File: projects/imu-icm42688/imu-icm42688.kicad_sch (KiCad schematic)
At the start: 14 parts, among them J1 HEADER, U1 AP2112K-3.3, U2 ICM-42688-P

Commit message: PCB workspace: scoped escape hatch, hardened gates, repo cleanup
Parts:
- removed C4: 100nF, Capacitor_SMD:C_0402_1005Metric, symbol Device:C
- removed C5: 1uF, Capacitor_SMD:C_0402_1005Metric, symbol Device:C
- removed J1: HEADER, Connector_PinHeader_2.54mm:PinHeader_1x10_P2.54mm_Vertical, symbol Connector_Generic:Conn_01x10
- removed R1, R2: 4.7k, Resistor_SMD:R_0402_1005Metric, symbol Device:R
- removed U1: AP2112K-3.3, Package_TO_SOT_SMD:SOT-23-5, symbol Regulator_Linear:AP2112K-3.3
- removed U2: ICM-42688-P, symbol Connector_Generic:Conn_01x14
- added J1: SPI-HDR, Connector_PinHeader_2.54mm:PinHeader_1x06_P2.54mm_Vertical, symbol Connector_Generic:Conn_01x06
- added TP3: INT1, TestPoint:TestPoint_Pad_1.0x1.0mm, symbol Connector_Generic:Conn_01x01
- added U1: ICM-42688-P, jlcpcb:LGA-14_L3.0-W2.5-P0.50-TL, symbol jlcpcb:ICM-42688-P
- C1: value 1uF -> 100nF
- C2: value 1uF -> 2.2uF; footprint Capacitor_SMD:C_0402_1005Metric -> Capacitor_SMD:C_0603_1608Metric
- C3: value 100nF -> 10nF
- H1, H2: value MH -> M2
- TP1: value TP_3V3 -> +3V3
- TP2: value TP_GND -> GND
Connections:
- net +3V3: now also C1.1, C2.1, C3.1, TP1.1 (Pin_1), J1.1 (Pin_1), U1.5 (VDDIO), U1.8 (VDD)
- net GND: now also C1.2, C2.2, C3.2, TP2.1 (Pin_1), J1.2 (Pin_2), U1.6 (GND), U1.7 (RESV), U1.9 (INT2/FSYNC/CLKIN)
- net INT1: now also TP3.1 (Pin_1), U1.4 (INT1/INT)
- new net SPI_CS: J1.6 (Pin_6), U1.12 (AP_CS)
- new net SPI_SCLK: J1.3 (Pin_3), U1.13 (AP_SCL/AP_SCLK)
- new net SPI_SDI: J1.4 (Pin_4), U1.14 (AP_SDA/AP_SDIO/AP_SDI)
- new net SPI_SDO: J1.5 (Pin_5), U1.1 (AP_SDO/AP_AD0)
- no-connect marks 0 -> 6

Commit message: 9/6 update
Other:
- company: (none) -> PSI Rocketry
- title: (none) -> IMU Breakout - ICM-42688-P
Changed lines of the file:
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@@
 	(generator_version "0.1")
 	(paper "A4")
+	(title_block
+		(title "IMU Breakout - ICM-42688-P")
+		(date "2026-08-24")
+		(rev "1")
+		(company "PSI Rocketry")
+		(comment 1 "Lee Taeho")
+	)
 	(sheet_instances
 		(path "/"
@@
 		(instances
 			(project "imu-icm42688"
-				(path "/b2c1d009-25c1-4b62-a2bc-4ddaf3d245d5"
+				(path "/22f1c0e7-3e2a-45f0-97f5-2cd534b13261"
 					(reference "U1")
 					(unit 1)
@@
 		(instances
 			(project "imu-icm42688"
-				(path "/b2c1d009-25c1-4b62-a2bc-4ddaf3d245d5"
+				(path "/22f1c0e7-3e2a-45f0-97f5-2cd534b13261"
 					(reference "#PWR101")
 					(unit 1)
@@
 		(instances
 			(project "imu-icm42688"
-				(path "/b2c1d009-25c1-4b62-a2bc-4ddaf3d245d5"
+				(path "/22f1c0e7-3e2a-45f0-97f5-2cd534b13261"
 					(reference "#PWR102")
 					(unit 1)
@@
 		(instances
 			(project "imu-icm42688"
-				(path "/b2c1d009-25c1-4b62-a2bc-4ddaf3d245d5"
+				(path "/22f1c0e7-3e2a-45f0-97f5-2cd534b13261"
 					(reference "#PWR103")
 					(unit 1)
@@
 		(instances
 			(project "imu-icm42688"
-				(path "/b2c1d009-25c1-4b62-a2bc-4ddaf3d245d5"
+				(path "/22f1c0e7-3e2a-45f0-97f5-2cd534b13261"
 					(reference "#PWR104")
 					(unit 1)
@@
 		(instances
 			(project "imu-icm42688"
-				(path "/b2c1d009-25c1-4b62-a2bc-4ddaf3d245d5"
+				(path "/22f1c0e7-3e2a-45f0-97f5-2cd534b13261"
 					(reference "#PWR105")
 					(unit 1)
@@
 		(instances
 			(project "imu-icm42688"
-				(path "/b2c1d009-25c1-4b62-a2bc-4ddaf3d245d5"
+				(path "/22f1c0e7-3e2a-45f0-97f5-2cd534b13261"
 					(reference "C1")
 					(unit 1)
@@
 		(instances
 			(project "imu-icm42688"
-				(path "/b2c1d009-25c1-4b62-a2bc-4ddaf3d245d5"
+				(path "/22f1c0e7-3e2a-45f0-97f5-2cd534b13261"
 					(reference "#PWR106")
 					(unit 1)
@@
 		(instances
 			(project "imu-icm42688"
-				(path "/b2c1d009-25c1-4b62-a2bc-4ddaf3d245d5"
+				(path "/22f1c0e7-3e2a-45f0-97f5-2cd534b13261"
 					(reference "#PWR107")
 					(unit 1)
@@
 		(instances
 			(project "imu-icm42688"
-				(path "/b2c1d009-25c1-4b62-a2bc-4ddaf3d245d5"
+				(path "/22f1c0e7-3e2a-45f0-97f5-2cd534b13261"
 					(reference "C2")
 					(unit 1)
@@
 		(instances
 			(project "imu-icm42688"
-				(path "/b2c1d009-25c1-4b62-a2bc-4ddaf3d245d5"
+				(path "/22f1c0e7-3e2a-45f0-97f5-2cd534b13261"
 					(reference "#PWR108")
 					(unit 1)
@@
 		(instances
 			(project "imu-icm42688"
-				(path "/b2c1d009-25c1-4b62-a2bc-4ddaf3d245d5"
+				(path "/22f1c0e7-3e2a-45f0-97f5-2cd534b13261"
 					(reference "#PWR109")
 					(unit 1)
@@
 		(instances
 			(project "imu-icm42688"
-				(path "/b2c1d009-25c1-4b62-a2bc-4ddaf3d245d5"
+				(path "/22f1c0e7-3e2a-45f0-97f5-2cd534b13261"
 					(reference "C3")
 					(unit 1)
@@
 		(instances
 			(project "imu-icm42688"
-				(path "/b2c1d009-25c1-4b62-a2bc-4ddaf3d245d5"
+				(path "/22f1c0e7-3e2a-45f0-97f5-2cd534b13261"
 					(reference "#PWR110")
 					(unit 1)
@@
 		(instances
 			(project "imu-icm42688"
-				(path "/b2c1d009-25c1-4b62-a2bc-4ddaf3d245d5"
+				(path "/22f1c0e7-3e2a-45f0-97f5-2cd534b13261"
 					(reference "#PWR111")
 					(unit 1)
@@
 		(instances
 			(project "imu-icm42688"
-				(path "/b2c1d009-25c1-4b62-a2bc-4ddaf3d245d5"
+				(path "/22f1c0e7-3e2a-45f0-97f5-2cd534b13261"
 					(reference "J1")
 					(unit 1)
@@
 		(instances
 			(project "imu-icm42688"
-				(path "/b2c1d009-25c1-4b62-a2bc-4ddaf3d245d5"
+				(path "/22f1c0e7-3e2a-45f0-97f5-2cd534b13261"
 					(reference "#PWR112")
 					(unit 1)
@@
 		(instances
 			(project "imu-icm42688"
-				(path "/b2c1d009-25c1-4b62-a2bc-4ddaf3d245d5"
+				(path "/22f1c0e7-3e2a-45f0-97f5-2cd534b13261"
 					(reference "#PWR113")
 					(unit 1)
@@
 		(instances
 			(project "imu-icm42688"
-				(path "/b2c1d009-25c1-4b62-a2bc-4ddaf3d245d5"
+				(path "/22f1c0e7-3e2a-45f0-97f5-2cd534b13261"
 					(reference "TP1")
 					(unit 1)
@@
 		(instances
 			(project "imu-icm42688"
-				(path "/b2c1d009-25c1-4b62-a2bc-4ddaf3d245d5"
+				(path "/22f1c0e7-3e2a-45f0-97f5-2cd534b13261"
 					(reference "#PWR114")
 					(unit 1)
@@
 		(instances
 			(project "imu-icm42688"
-				(path "/b2c1d009-25c1-4b62-a2bc-4ddaf3d245d5"
+				(path "/22f1c0e7-3e2a-45f0-97f5-2cd534b13261"
 					(reference "TP2")
 					(unit 1)
@@
 		(instances
 			(project "imu-icm42688"
-				(path "/b2c1d009-25c1-4b62-a2bc-4ddaf3d245d5"
+				(path "/22f1c0e7-3e2a-45f0-97f5-2cd534b13261"
 					(reference "#PWR115")
 					(unit 1)
@@
 		(instances
 			(project "imu-icm42688"
-				(path "/b2c1d009-25c1-4b62-a2bc-4ddaf3d245d5"
+				(path "/22f1c0e7-3e2a-45f0-97f5-2cd534b13261"
 					(reference "TP3")
 					(unit 1)
@@
 		(instances
 			(project "imu-icm42688"
-				(path "/b2c1d009-25c1-4b62-a2bc-4ddaf3d245d5"
+				(path "/22f1c0e7-3e2a-45f0-97f5-2cd534b13261"
 					(reference "#FLG01")
 					(unit 1)
@@
 		(instances
 			(project "imu-icm42688"
-				(path "/b2c1d009-25c1-4b62-a2bc-4ddaf3d245d5"
+				(path "/22f1c0e7-3e2a-45f0-97f5-2cd534b13261"
 					(reference "#PWR116")
 					(unit 1)
@@
 		(instances
 			(project "imu-icm42688"
-				(path "/b2c1d009-25c1-4b62-a2bc-4ddaf3d245d5"
+				(path "/22f1c0e7-3e2a-45f0-97f5-2cd534b13261"
 					(reference "#FLG02")
 					(unit 1)
@@
 		(instances
 			(project "imu-icm42688"
-				(path "/b2c1d009-25c1-4b62-a2bc-4ddaf3d245d5"
+				(path "/22f1c0e7-3e2a-45f0-97f5-2cd534b13261"
 					(reference "#PWR117")
 					(unit 1)
@@
 		(instances
 			(project "imu-icm42688"
-				(path "/b2c1d009-25c1-4b62-a2bc-4ddaf3d245d5"
+				(path "/22f1c0e7-3e2a-45f0-97f5-2cd534b13261"
 					(reference "H1")
 					(unit 1)
@@
 		(instances
 			(project "imu-icm42688"
-				(path "/b2c1d009-25c1-4b62-a2bc-4ddaf3d245d5"
+				(path "/22f1c0e7-3e2a-45f0-97f5-2cd534b13261"
 					(reference "H2")
 					(unit 1)

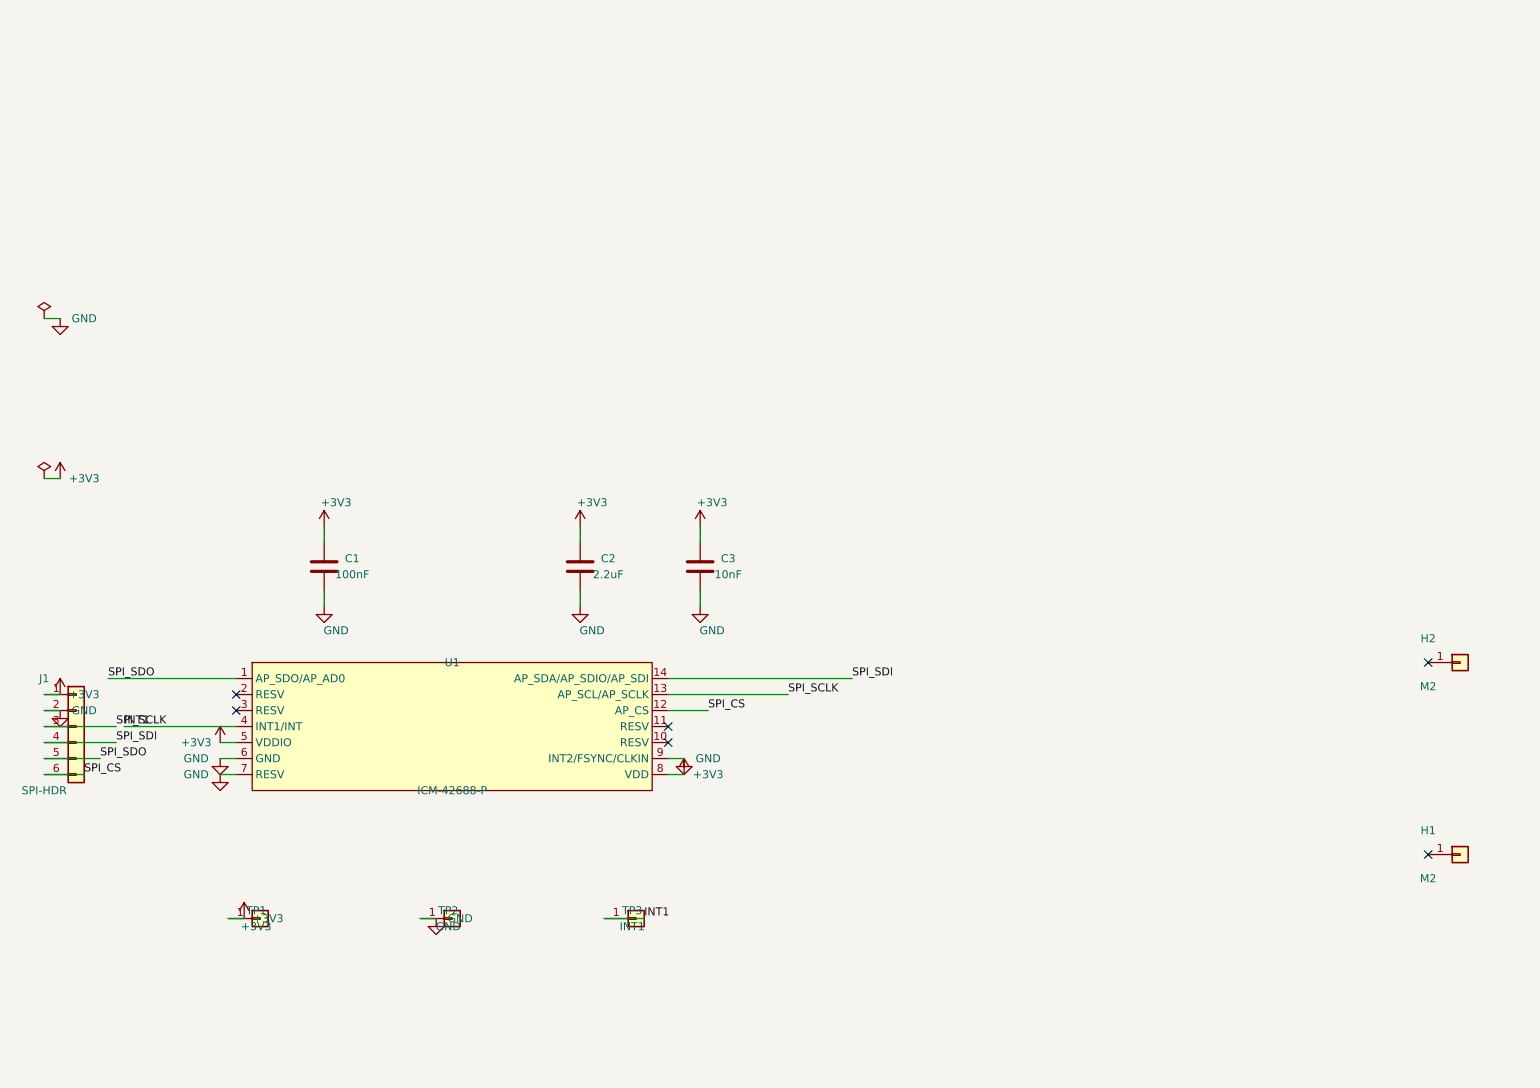
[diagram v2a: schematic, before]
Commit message: feat: promote IMU and GNSS working schematics
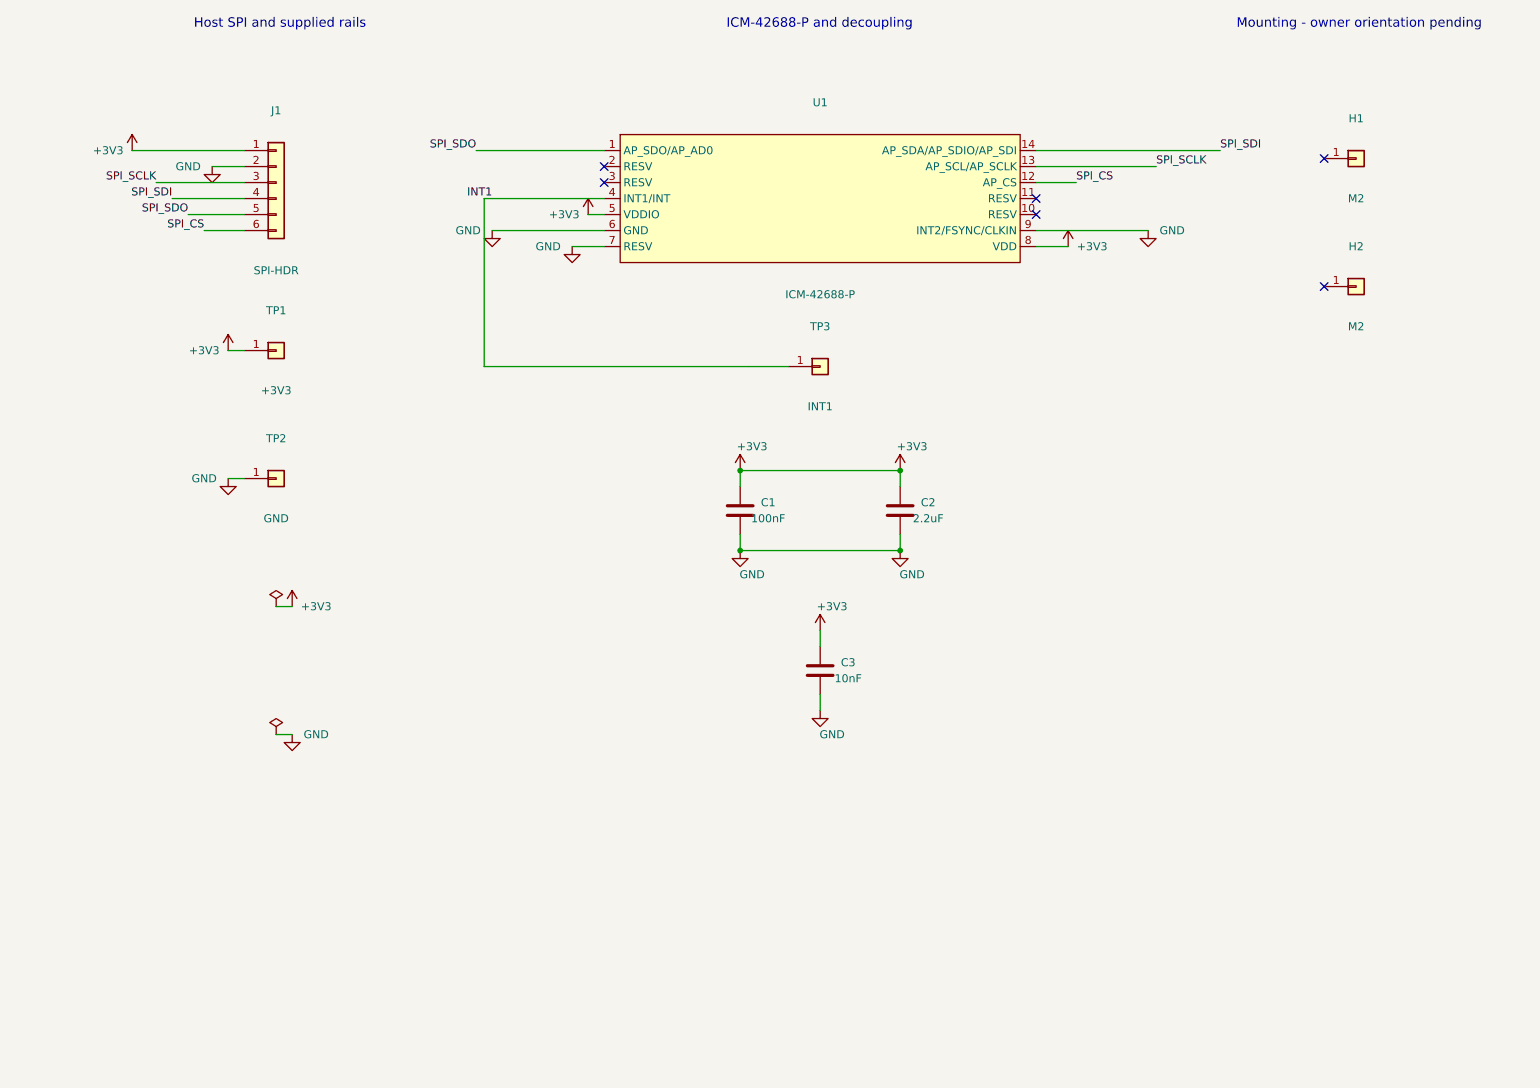
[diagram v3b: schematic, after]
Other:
- note added: "Host SPI and supplied rails"
- note added: "ICM-42688-P and decoupling"
- note added: "Mounting - owner orientation pending"
- company: PSI Rocketry -> (none)
- title: IMU Breakout - ICM-42688-P -> ICM-42688-P SPI breakout
